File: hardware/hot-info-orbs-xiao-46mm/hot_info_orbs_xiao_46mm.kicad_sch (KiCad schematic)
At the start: 12 parts, among them SW1 SW_Push, SW2 SW_Push, SW3 SW_Push, U2 XIAO ESP32-S3 Plus

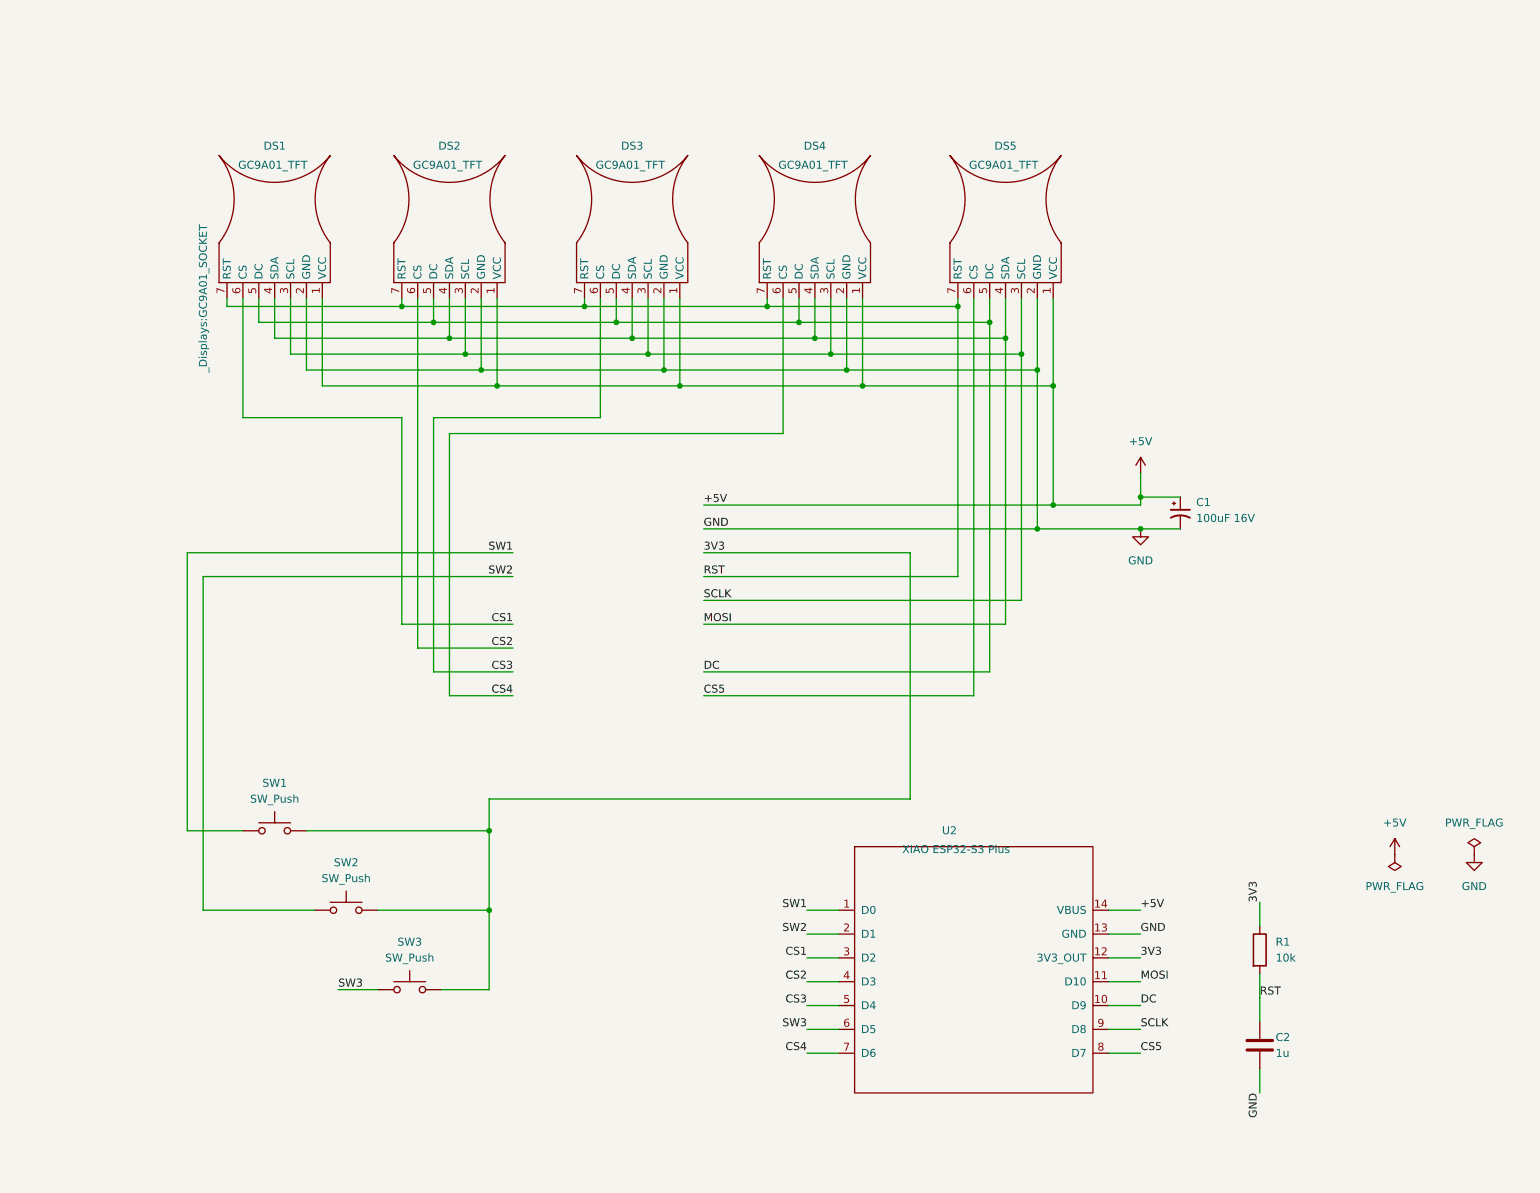
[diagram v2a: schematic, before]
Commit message: 46mm schematic: Scott's layout cleanup, title block to rev 2.4, one SW3 track straightened
Scott tidied the sheet on 2026-10-23. The edits sat uncommitted, so the package
sent to Yang that afternoon (built from 8dda9b9) still had the old layout:
U2 and the R1/C2 reset circuit sat apart from the rest and overlapped the title
block, which Yang read as "disconnected".

Connectivity is unchanged. XML netlists of 8dda9b9 and this commit have the
same 12 parts and the same 15 nets, pin for pin. ERC is 0. DRC shows the 3
known XIAO USB-C silk warnings, 0 unconnected, 0 parity. Board: one /SW3
dogleg near (123.5, 92.8) is now a direct run, and the pour was refilled.

Committed as Scott saved it, not re-laid out by script: the layout is his and
the netlist check is what shows it is safe.

Co-Authored-By: Claude Opus 5.5 <noreply@anthropic.com>
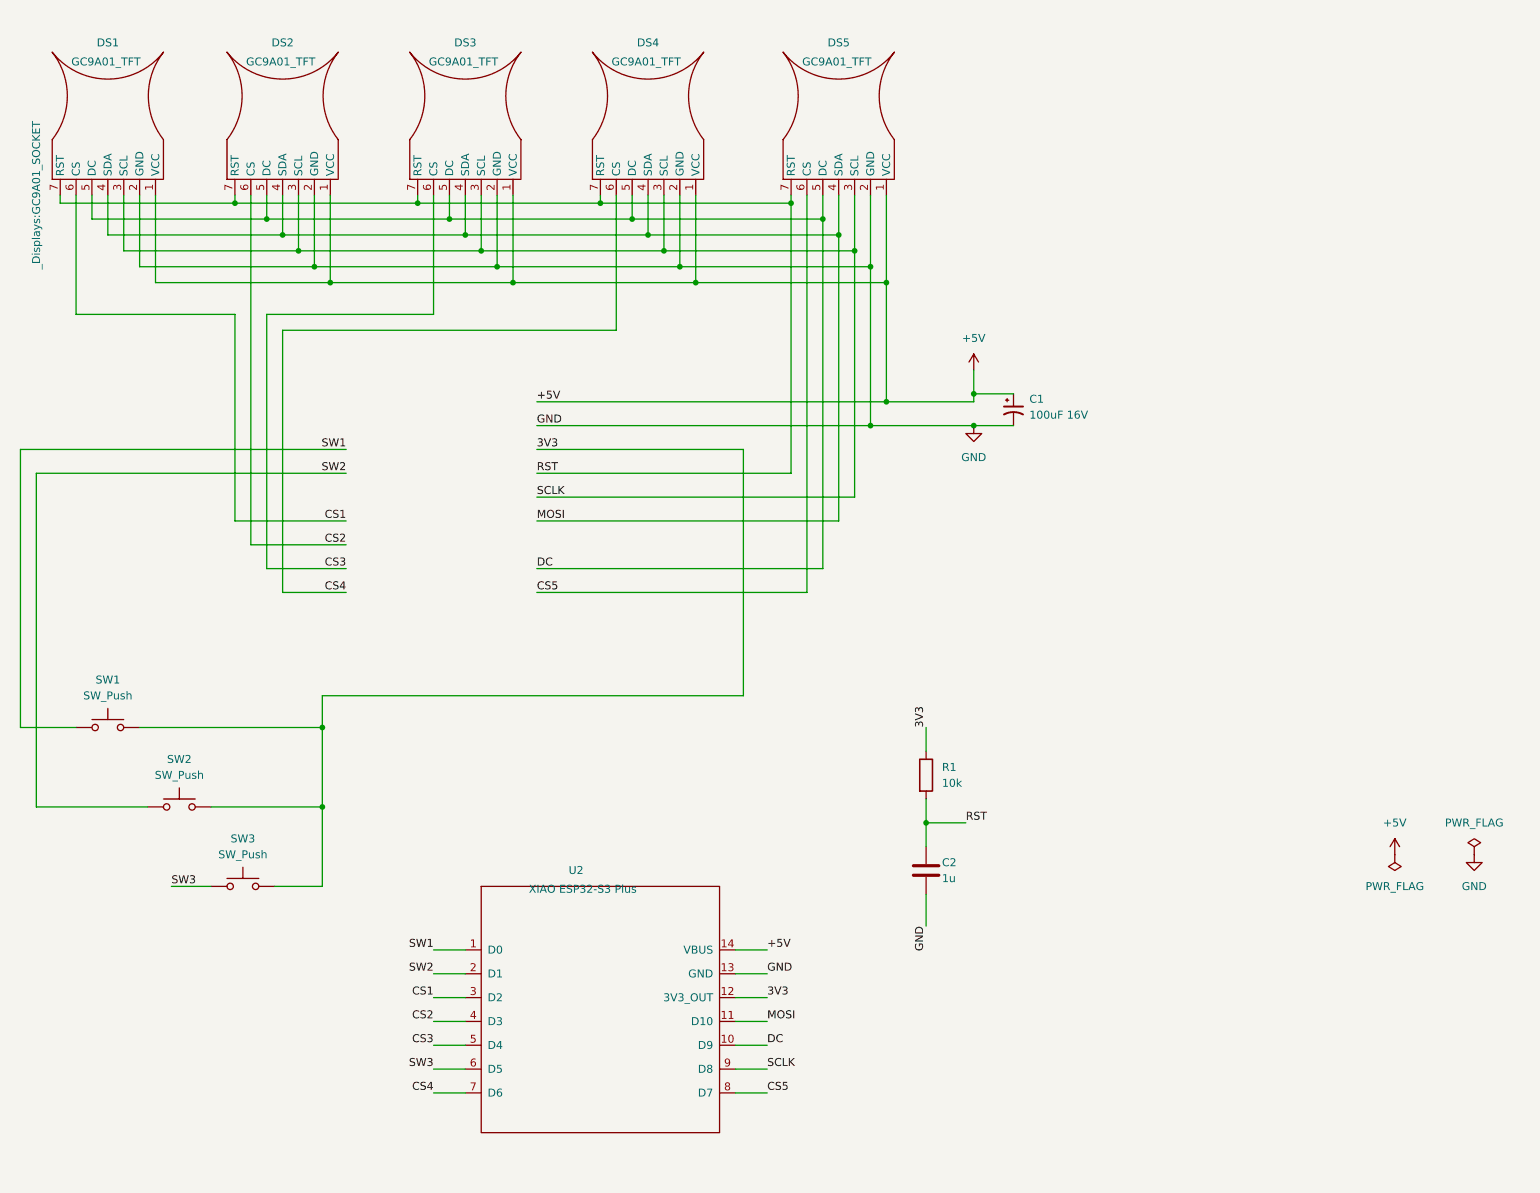
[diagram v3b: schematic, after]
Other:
- moved on the sheet: C1, C2, DS1, DS2, DS3, DS4, DS5, R1, SW1, SW2, SW3, U2

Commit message: 46mm schematic: displays as a labelled block, no wires across the page
Each display pin now has a short stub and its net label, the five displays
sit in a dashed box, and the mid-sheet label column is gone. SW1/SW2 get
labels at the switch like SW3, and the switch bus a 3V3 label. 136 wires,
junctions and labels out, 78 in, by tools/display_block.py; no symbol moved.

Checked against HEAD: kicadxml netlist identical (net names and pins),
ERC 0, DRC 3 known silk warnings / 0 unconnected / 0 parity.

Rejected a hierarchical sheet for the displays: Scott chose a boxed group on
the same page, and a sub-sheet would change every display's symbol path and
need the PCB re-linked. Dropped the +5V/GND labels at C1 too: a label joins
the power net by name, so the netlist is the same without them.

Co-Authored-By: Claude Opus 5.5 <noreply@anthropic.com>
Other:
- note added: "DISPLAYS DS1-DS5: GC9A01 round TFT, each in a 1x7 socket"

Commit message: 46mm schematic: box and title every circuit group like DISPLAYS
Scott asked for each discrete group in its own dashed box, titled inside
the bottom-left corner as DISPLAYS is: MCU, BUTTONS, DISPLAY RESET,
5V BULK and POWER FLAGS. tools/group_boxes.py sizes each box from what
KiCad draws for the group (body graphics, visible fields with their
justification, the wires and labels hanging off its pins), so a later
layout change is one re-run, which replaces the boxes it drew.

Rejected: drawing the boxes by hand in eeschema. It cannot be re-run
after a layout change and gives no overlap check; the script reports
any box that crosses another.

Graphics only. Checked against HEAD: kicadxml netlist identical by net
name and pins, components identical, ERC 0, DRC 0 unconnected and
0 parity (the 3 known silk warnings unchanged).

Co-Authored-By: Claude Opus 5.5 <noreply@anthropic.com>
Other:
- note added: "5V BULK C1"
- note added: "BUTTONS SW1-SW3: tact switches to 3V3"
- note added: "DISPLAY RESET R1/C2: RC power-on"
- note added: "MCU U2: XIAO ESP32-S3 or S3 Plus"
- note added: "POWER FLAGS ERC only"
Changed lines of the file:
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@@
+		)
+	)
+	(rectangle
+		(start 76.2 147.32)
+		(end 146.05 201.93)
+		(stroke
+			(width 0)
+			(type dash)
+		)
+		(fill
+			(type none)
+		)
+	)
+	(text "MCU  U2: XIAO ESP32-S3 or S3 Plus"
+		(exclude_from_sim no)
+		(at 77.47 200.66 0)
+		(effects
+			(font
+				(size 1.27 1.27)
+			)
+			(justify left bottom)
+		)
+	)
+	(rectangle
+		(start 17.78 114.3)
+		(end 71.12 162.56)
+		(stroke
+			(width 0)
+			(type dash)
+		)
+		(fill
+			(type none)
+		)
+	)
+	(text "BUTTONS  SW1-SW3: tact switches to 3V3"
+		(exclude_from_sim no)
+		(at 19.05 161.29 0)
+		(effects
+			(font
+				(size 1.27 1.27)
+			)
+			(justify left bottom)
+		)
+	)
+	(rectangle
+		(start 157.48 121.92)
+		(end 196.85 171.45)
+		(stroke
+			(width 0)
+			(type dash)
+		)
+		(fill
+			(type none)
+		)
+	)
+	(text "DISPLAY RESET  R1/C2: RC power-on"
+		(exclude_from_sim no)
+		(at 158.75 170.18 0)
+		(effects
+			(font
+				(size 1.27 1.27)
+			)
+			(justify left bottom)
+		)
+	)
+	(rectangle
+		(start 165.1 63.5)
+		(end 191.77 92.71)
+		(stroke
+			(width 0)
+			(type dash)
+		)
+		(fill
+			(type none)
+		)
+	)
+	(text "5V BULK  C1"
+		(exclude_from_sim no)
+		(at 166.37 91.44 0)
+		(effects
+			(font
+				(size 1.27 1.27)
+			)
+			(justify left bottom)
+		)
+	)
+	(rectangle
+		(start 229.87 140.97)
+		(end 257.81 161.29)
+		(stroke
+			(width 0)
+			(type dash)
+		)
+		(fill
+			(type none)
+		)
+	)
+	(text "POWER FLAGS  ERC only"
+		(exclude_from_sim no)
+		(at 231.14 160.02 0)
+		(effects
+			(font
+				(size 1.27 1.27)
+			)
+			(justify left bottom)
 		)
 	)
